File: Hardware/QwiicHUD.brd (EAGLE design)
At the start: 25.4 x 34.3 mm, 48 parts, among them J4 WISECHIP_HUD_FPC, U1 AP3012

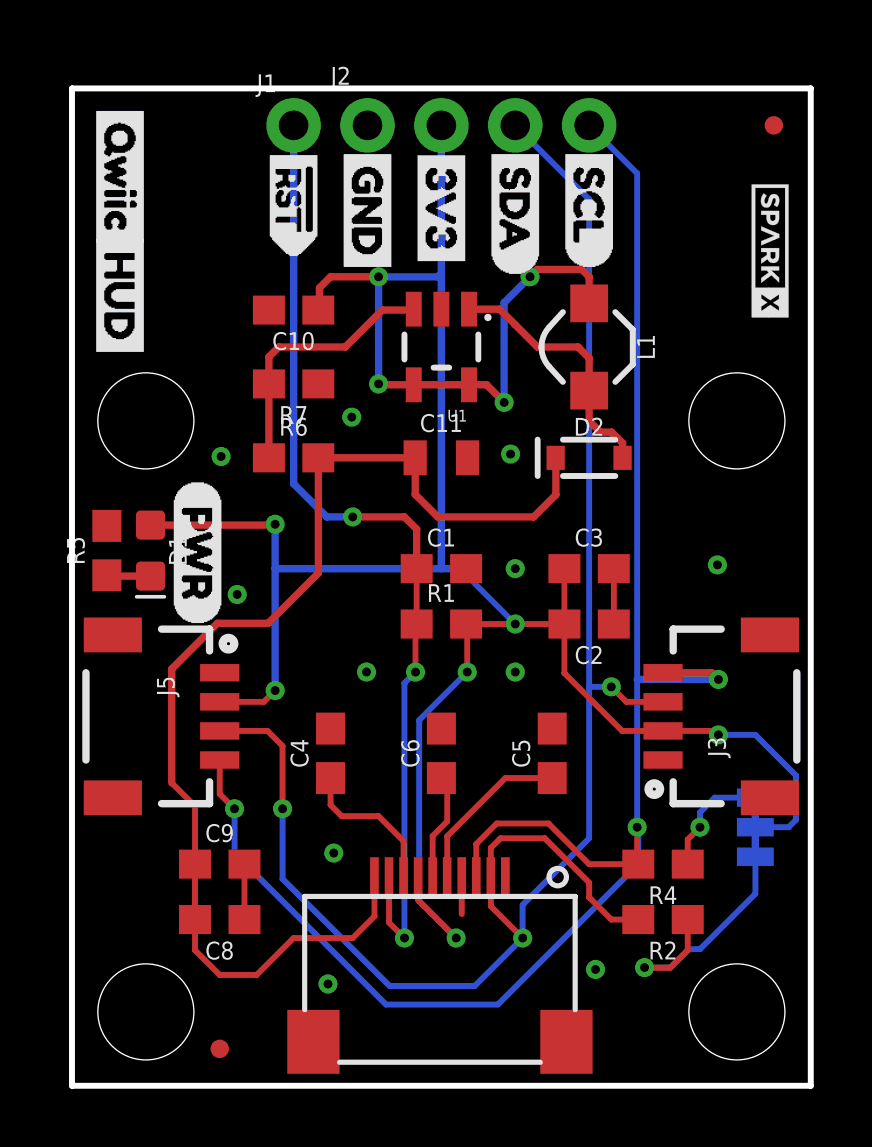
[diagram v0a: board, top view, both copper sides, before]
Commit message: Revert "Changed inductor to inventory part"
This reverts commit 6ab7a03f3320a090153a192dfaf0fd3f0c8c93f1.
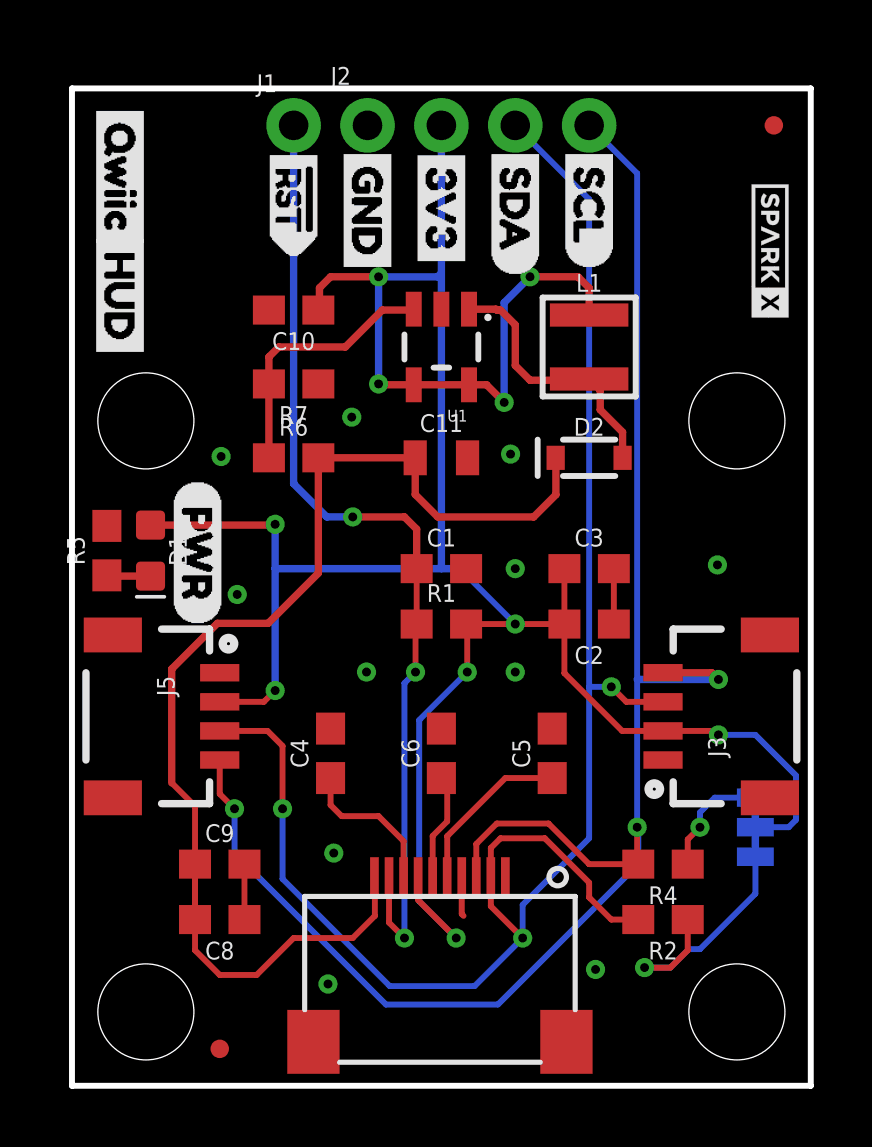
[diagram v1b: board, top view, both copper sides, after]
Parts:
- L1: device SparkFun-Coils:INDUCTOR_4.7UH -> 1.81_Greyscale_OLED_Breakout:INDUCTOR_3X3
- turned L1 to 0 degrees
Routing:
- net 3.3V: track 91.8 -> 93.0 mm
